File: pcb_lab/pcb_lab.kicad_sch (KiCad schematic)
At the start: 1 part

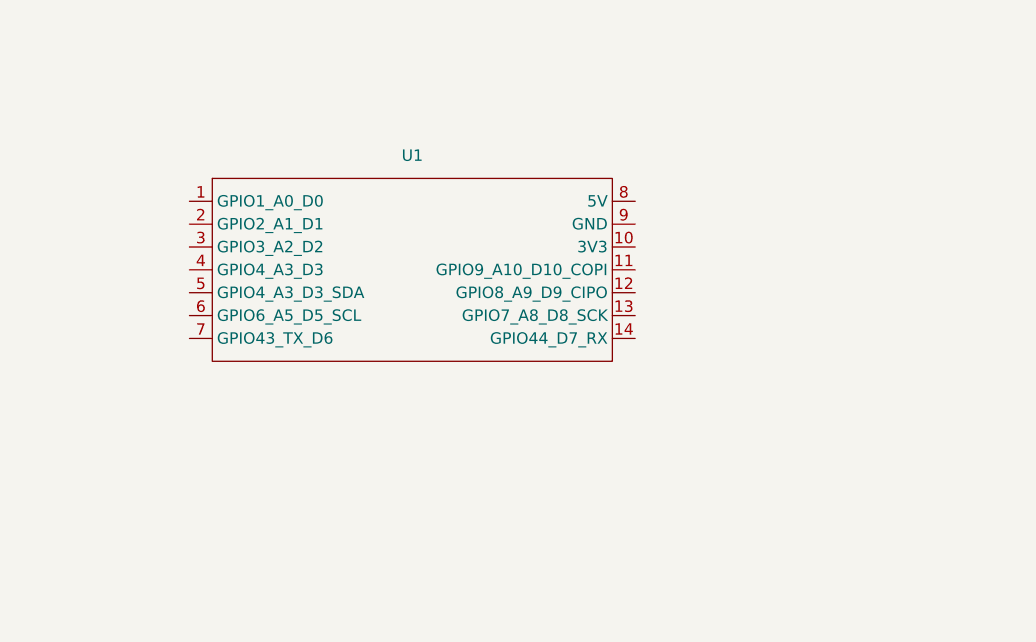
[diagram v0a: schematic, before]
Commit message: Modify pcb_lab related documents
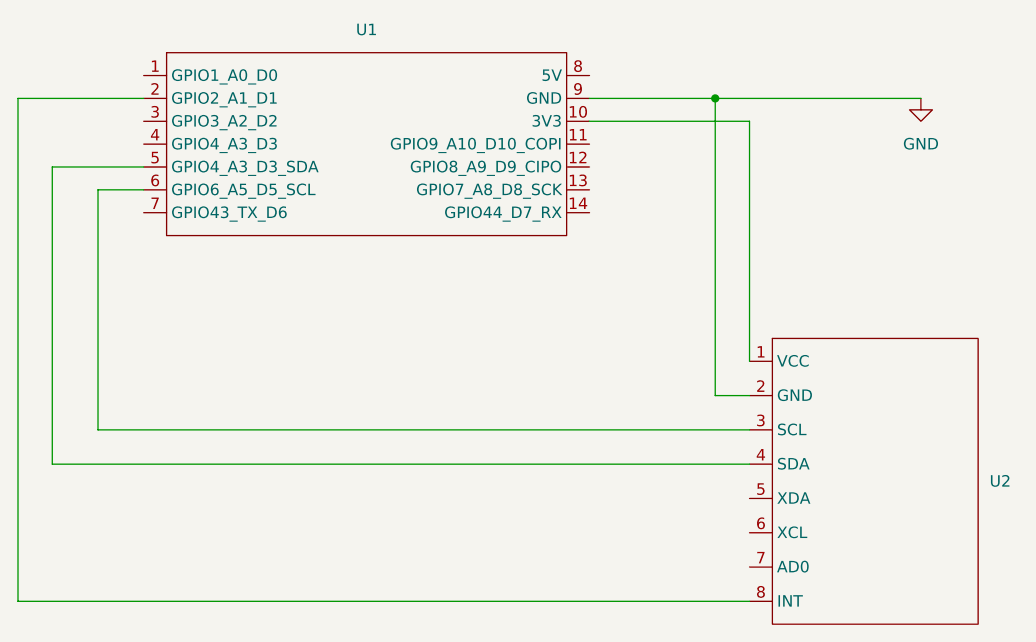
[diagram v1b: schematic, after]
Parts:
- added U2: ~, symbol TECHIN514_FinalProject_Library:MPU6050
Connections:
- net at U1.10 (3V3): now also U2.1 (VCC)
- net at U1.2 (GPIO2_A1_D1): now also U2.8 (INT)
- net at U1.5 (GPIO4_A3_D3_SDA): now also U2.4 (SDA)
- net at U1.6 (GPIO6_A5_D5_SCL): now also U2.3 (SCL)
- net GND: now reaches U1.9 (GND)
- net GND: now also U2.2 (GND)
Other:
- moved on the sheet: U1
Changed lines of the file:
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@@
 (kicad_sch (version 20230121) (generator eeschema)
   (paper "A4")
-  (symbol (lib_id "ESP32:XIAO_ESP32_SENSE") (at 127 95.25 0) (unit 1)
+  (junction (at 162.56 77.47) (diameter 0) (color 0 0 0 0)
+  )
+  (wire (pts (xy 166.37 133.35) (xy 85.09 133.35))
+    (stroke (width 0) (type default))
+  )
+  (wire (pts (xy 99.06 87.63) (xy 93.98 87.63))
+    (stroke (width 0) (type default))
+  )
+  (wire (pts (xy 162.56 110.49) (xy 166.37 110.49))
+    (stroke (width 0) (type default))
+  )
+  (wire (pts (xy 93.98 114.3) (xy 166.37 114.3))
+    (stroke (width 0) (type default))
+  )
+  (wire (pts (xy 162.56 77.47) (xy 185.42 77.47))
+    (stroke (width 0) (type default))
+  )
+  (wire (pts (xy 166.37 80.01) (xy 166.37 106.68))
+    (stroke (width 0) (type default))
+  )
+  (wire (pts (xy 85.09 133.35) (xy 85.09 77.47))
+    (stroke (width 0) (type default))
+  )
+  (wire (pts (xy 148.59 77.47) (xy 162.56 77.47))
+    (stroke (width 0) (type default))
+  )
+  (wire (pts (xy 162.56 77.47) (xy 162.56 110.49))
+    (stroke (width 0) (type default))
+  )
+  (wire (pts (xy 88.9 85.09) (xy 88.9 118.11))
+    (stroke (width 0) (type default))
+  )
+  (wire (pts (xy 148.59 80.01) (xy 166.37 80.01))
+    (stroke (width 0) (type default))
+  )
+  (wire (pts (xy 93.98 87.63) (xy 93.98 114.3))
+    (stroke (width 0) (type default))
+  )
+  (wire (pts (xy 85.09 77.47) (xy 99.06 77.47))
+    (stroke (width 0) (type default))
+  )
+  (wire (pts (xy 99.06 85.09) (xy 88.9 85.09))
+    (stroke (width 0) (type default))
+  )
+  (wire (pts (xy 88.9 118.11) (xy 166.37 118.11))
+    (stroke (width 0) (type default))
+  )
+  (symbol (lib_id "ESP32:XIAO_ESP32_SENSE") (at 121.92 81.28 0) (unit 1)
     (in_bom yes) (on_board yes) (dnp no) (fields_autoplaced)
-    (property "Reference" "U1" (at 128.905 83.82 0)
+    (property "Reference" "U1" (at 123.825 69.85 0)
       (effects (font (size 1.27 1.27)))
     )
-    (property "Value" "~" (at 127 95.25 0)
+    (property "Value" "~" (at 121.92 81.28 0)
       (effects (font (size 1.27 1.27)))
     )
-    (property "Footprint" "ESP32:XIAO_ESP32_SENSE" (at 127 95.25 0)
+    (property "Footprint" "ESP32:XIAO_ESP32_SENSE" (at 121.92 81.28 0)
       (effects (font (size 1.27 1.27)) hide)
     )
-    (property "Datasheet" "" (at 127 95.25 0)
+    (property "Datasheet" "" (at 121.92 81.28 0)
       (effects (font (size 1.27 1.27)) hide)
     )
@@
         )
       )
+    )
+  )
+  (symbol (lib_id "power:GND") (at 185.42 77.47 0) (unit 1)
+    (in_bom yes) (on_board yes) (dnp no) (fields_autoplaced)
+    (property "Reference" "#PWR01" (at 185.42 83.82 0)
+      (effects (font (size 1.27 1.27)) hide)
+    )
+    (property "Value" "GND" (at 185.42 82.55 0)
+      (effects (font (size 1.27 1.27)))
+    )
+    (property "Footprint" "" (at 185.42 77.47 0)
+      (effects (font (size 1.27 1.27)) hide)
+    )
+    (property "Datasheet" "" (at 185.42 77.47 0)
+      (effects (font (size 1.27 1.27)) hide)
+    )
+    (pin "1")
+    (instances
+      (project "pcb_lab"
+        (path "/672b6a17-686d-4fea-90cf-e1054621ca99"
+          (reference "#PWR01") (unit 1)
+        )
+      )
+    )
+  )
+  (symbol (lib_id "TECHIN514_FinalProject_Library:MPU6050") (at 171.45 101.6 0) (unit 1)
+    (in_bom yes) (on_board yes) (dnp no) (fields_autoplaced)
+    (property "Reference" "U2" (at 193.04 120.015 0)
+      (effects (font (size 1.27 1.27)) (justify left))
+    )
+    (property "Value" "~" (at 171.45 97.79 0)
+      (effects (font (size 1.27 1.27)))
+    )
+    (property "Footprint" "" (at 171.45 97.79 0)
+      (effects (font (size 1.27 1.27)) hide)
+    )
+    (property "Datasheet" "" (at 171.45 97.79 0)
+      (effects (font (size 1.27 1.27)) hide)
+    )
+    (pin "2")
+    (pin "7")
+    (pin "4")
+    (pin "3")
+    (pin "8")
+    (pin "5")
+    (pin "1")
+    (pin "6")
+    (instances
+      (project "pcb_lab"
+        (path "/672b6a17-686d-4fea-90cf-e1054621ca99"
+          (reference "U2") (unit 1)
+        )
+      )

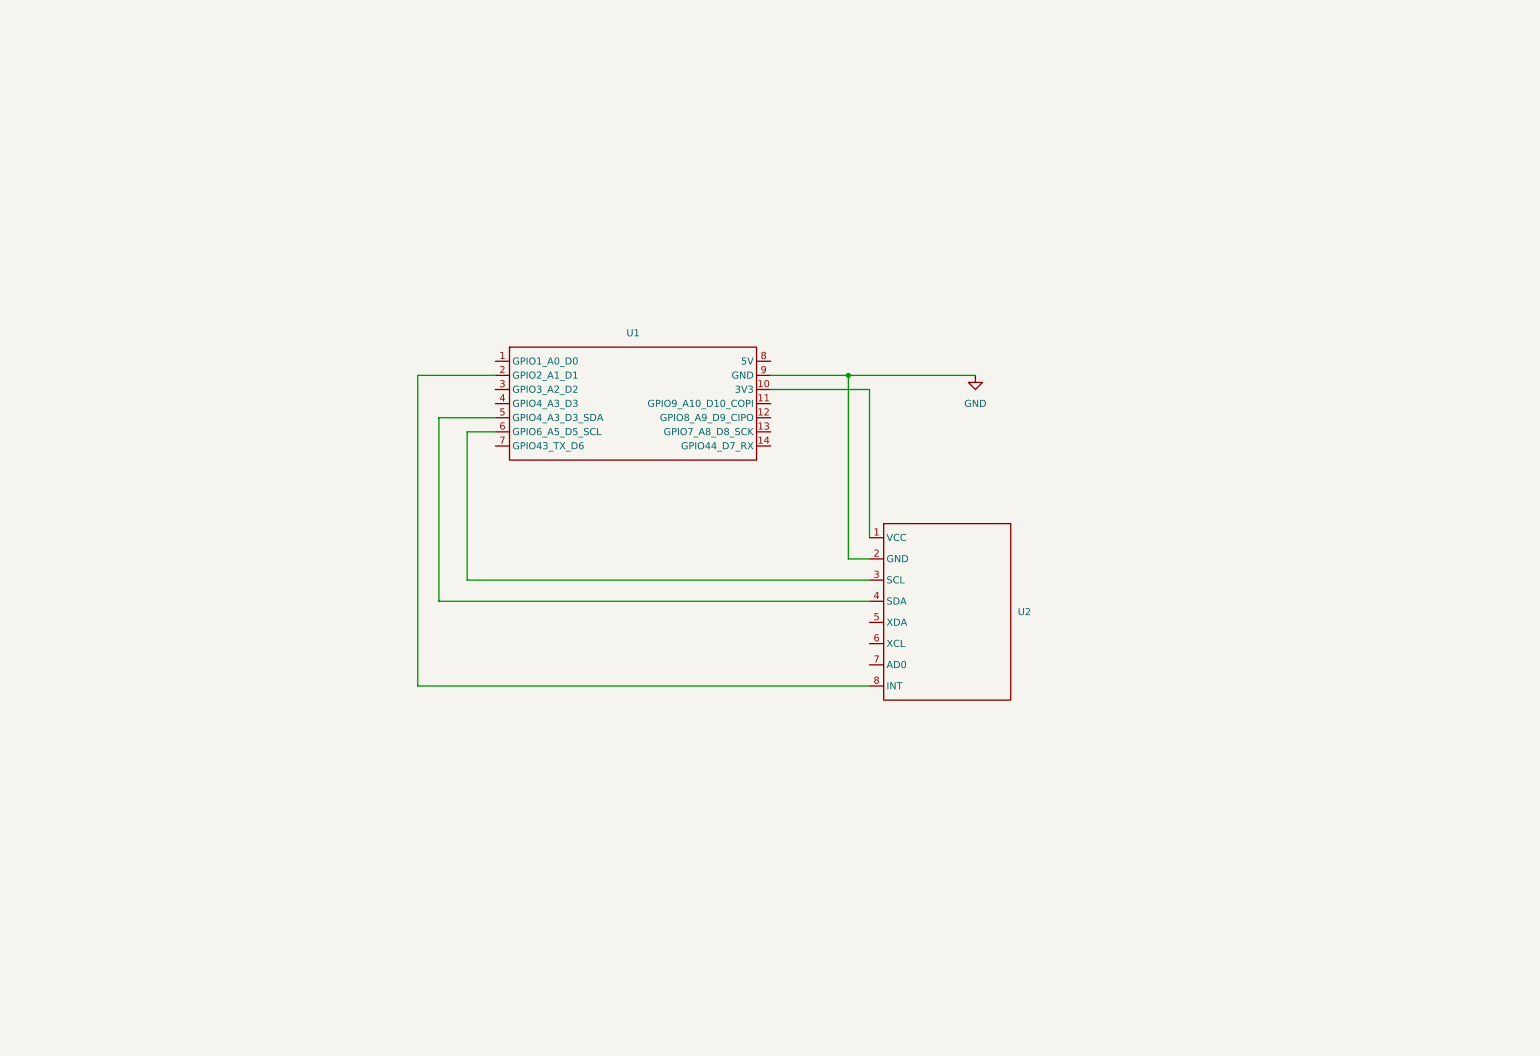
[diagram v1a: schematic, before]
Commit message: update with battery estimate
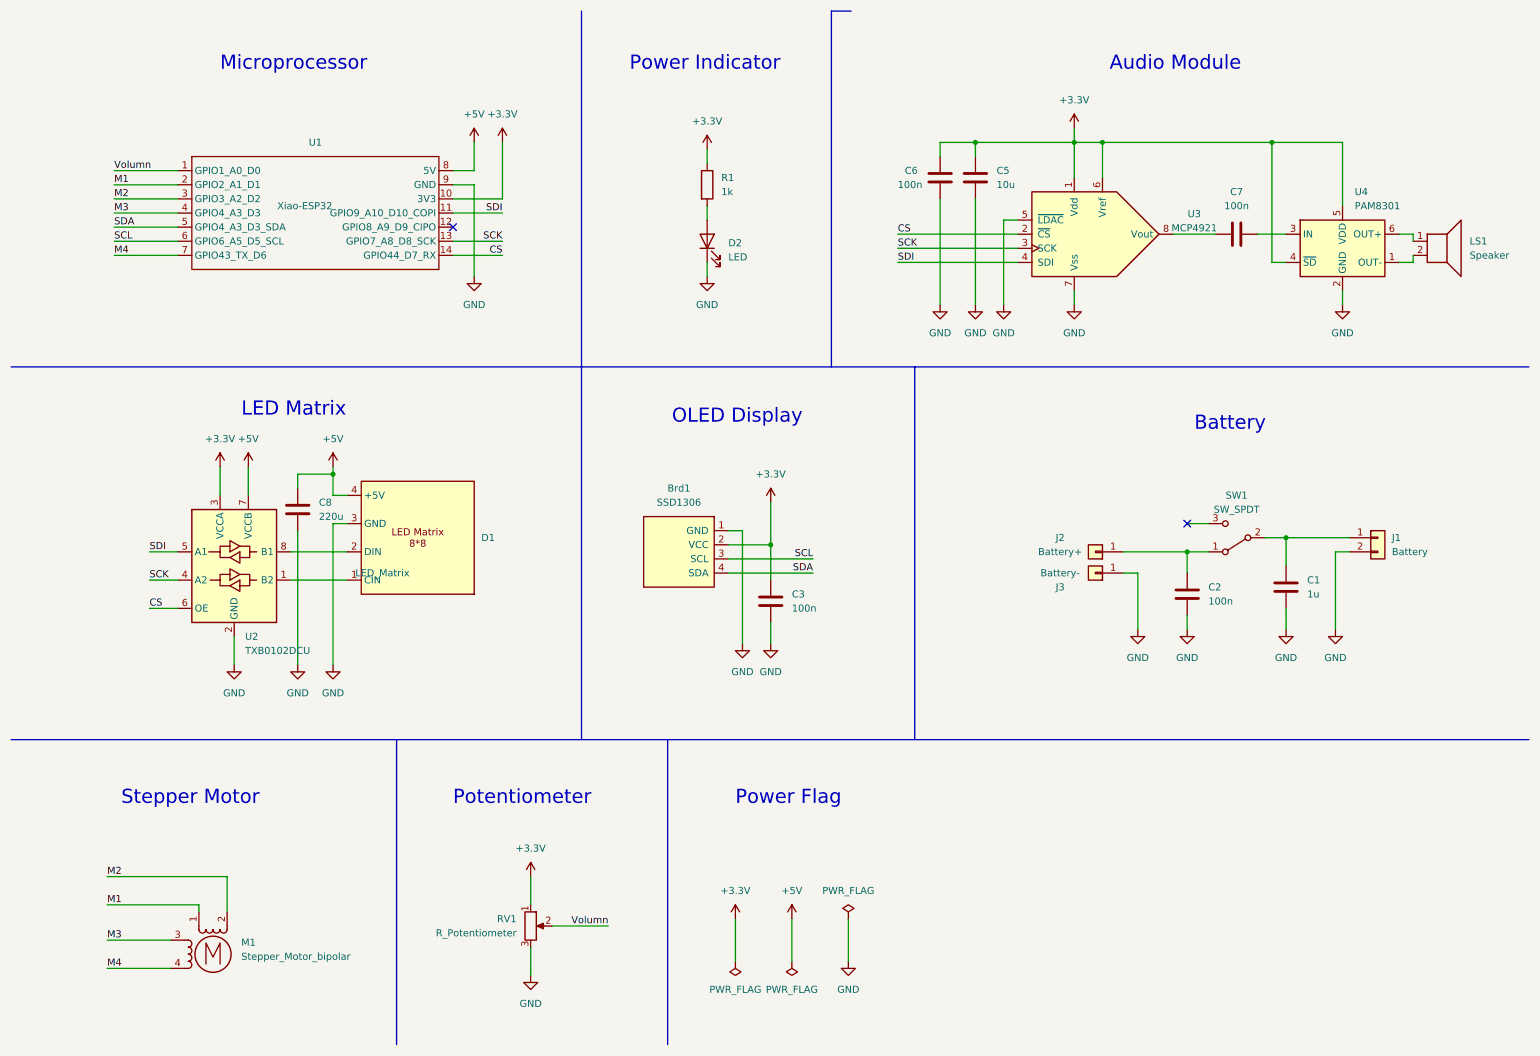
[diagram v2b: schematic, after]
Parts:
- removed U2: ~, symbol TECHIN514_FinalProject_Library:MPU6050
- added Brd1: SSD1306, Library:128x64OLED, symbol ssd1306:SSD1306
- added C1: 1u, Capacitor_SMD:C_0603_1608Metric_Pad1.08x0.95mm_HandSolder, symbol Device:C
- added C2, C3, C6, C7: 100n, Capacitor_SMD:C_0603_1608Metric_Pad1.08x0.95mm_HandSolder, symbol Device:C
- added C5: 10u, Capacitor_Tantalum_SMD:CP_EIA-1608-08_AVX-J_Pad1.25x1.05mm_HandSolder, symbol Device:C
- added C8: 220u, Capacitor_THT:CP_Radial_D8.0mm_P3.80mm, symbol Device:C
- added D1: LED_Matrix, Connector_PinSocket_2.54mm:PinSocket_1x04_P2.54mm_Horizontal, symbol Dotstar8x8:DotStar
- added D2: LED, LED_SMD:LED_0603_1608Metric_Pad1.05x0.95mm_HandSolder, symbol Device:LED
- added J1: Battery, Connector_JST:JST_PH_S2B-PH-SM4-TB_1x02-1MP_P2.00mm_Horizontal, symbol Connector_Generic:Conn_01x02
- added J2: Battery+, TestPoint:TestPoint_Pad_D2.5mm, symbol Connector_Generic:Conn_01x01
- added J3: Battery-, TestPoint:TestPoint_Pad_D2.5mm, symbol Connector_Generic:Conn_01x01
- added LS1: Speaker, Connector_JST:JST_NV_B02P-NV_1x02_P5.00mm_Vertical, symbol Device:Speaker
- added M1: Stepper_Motor_bipolar, Library:X27_stepper_motor, symbol Motor:Stepper_Motor_bipolar
- added R1: 1k, Resistor_SMD:R_0603_1608Metric_Pad0.98x0.95mm_HandSolder, symbol Device:R
- added RV1: R_Potentiometer, Potentiometer_THT:Potentiometer_Piher_PC-16_Single_Horizontal, symbol Device:R_Potentiometer
- added SW1: SW_SPDT, Connector_JST:JST_EH_B3B-EH-A_1x03_P2.50mm_Vertical, symbol Switch:SW_SPDT
- added U2: TXB0102DCU, Package_SO:VSSOP-8_2.4x2.1mm_P0.5mm, symbol Logic_LevelTranslator:TXB0102DCU
- added U3: MCP4921, Package_DFN_QFN:DFN-8-1EP_3x2mm_P0.5mm_EP1.3x1.5mm, symbol Analog_DAC:MCP4921
- added U4: PAM8301, Package_TO_SOT_SMD:SOT-23-6, symbol Amplifier_Audio:PAM8301
- U1: value ~ -> Xiao-ESP32; footprint ESP32:XIAO_ESP32_SENSE -> Library:XIAO_ESP32_SENSE
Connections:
- net GND: now also Brd1.1 (GND), C1.2, C2.2, C3.2, C5.2, C6.2, C8.2, D1.3 (GND), D2.1 (K), J1.2 (Pin_2), J3.1 (Pin_1), RV1.3, U2.2 (GND), U3.5 (~{LDAC}), U3.7 (Vss), U4.2 (GND)
- net Volumn: now reaches U1.1 (GPIO1_A0_D0)
- net Volumn: now also RV1.2
- net +3.3V: now reaches U1.10 (3V3)
- net +3.3V: now also Brd1.2 (VCC), C3.1, C5.1, C6.1, R1.1, RV1.1, U2.3 (VCCA), U3.1 (Vdd), U3.6 (Vref), U4.4 (~{SD}), U4.5 (VDD)
- net SDI: now reaches U1.11 (GPIO9_A10_D10_COPI)
- net SDI: now also U2.5 (A1), U3.4 (SDI)
- net SCK: now reaches U1.13 (GPIO7_A8_D8_SCK)
- net SCK: now also U2.4 (A2), U3.3 (SCK)
- net CS: now reaches U1.14 (GPIO44_D7_RX)
- net CS: now also U2.6 (OE), U3.2 (~{CS})
- net M1: now reaches U1.2 (GPIO2_A1_D1)
- net M1: now also M1.1
- net M2: now reaches U1.3 (GPIO3_A2_D2)
- net M2: now also M1.2 (-)
- net M3: now reaches U1.4 (GPIO4_A3_D3)
- net M3: now also M1.3
- net SDA: now reaches U1.5 (GPIO4_A3_D3_SDA)
- net SDA: now also Brd1.4 (SDA)
- net SCL: now reaches U1.6 (GPIO6_A5_D5_SCL)
- net SCL: now also Brd1.3 (SCL)
- net M4: now reaches U1.7 (GPIO43_TX_D6)
- net M4: now also M1.4
- net +5V: now reaches U1.8 (5V)
- net +5V: now also C8.1, D1.4 (+5V), U2.7 (VCCB)
- new net: D2.2 (A), R1.2
- new net: C1.1, J1.1 (Pin_1), SW1.2 (B)
- new net: C2.1, J2.1 (Pin_1), SW1.1 (A)
- new net: C7.1, U3.8 (Vout)
- new net: C7.2, U4.3 (IN)
- new net: D1.1 (CIN), U2.1 (B2)
- new net: D1.2 (DIN), U2.8 (B1)
- new net: LS1.1, U4.6 (OUT+)
- new net: LS1.2, U4.1 (OUT-)
- no-connect marks 0 -> 2
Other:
- note added: "Audio Module"
- note added: "Battery"
- note added: "LED Matrix"
- note added: "Microprocessor"
- note added: "OLED Display"
- note added: "Potentiometer"
- note added: "Power Flag"
- note added: "Power Indicator"
- note added: "Stepper Motor"
- company: (none) -> Wanling Yu
- title: (none) -> Display-device Demo
- moved on the sheet: U1
